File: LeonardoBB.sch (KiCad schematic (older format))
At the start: 39 parts, among them J1 USB_B_Micro, J2 Conn_01x17, J3 Conn_01x17, J4 I2C, Q1 Q_PMOS_GSD, Q2 Q_DUAL_PMOS_S1G1D2S2G2D1, SW1 SW_SPDT, U1 ATmega32U4-MU, U2 LMV358, U3 NCP1117-5.0_SOT223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

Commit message: Change footprints for USB and LMV358
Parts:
- J1: footprint Connector_USB:USB_Micro-B_Amphenol_10103594-0001LF_Horizontal -> Connector_USB:USB_Micro-B_Molex-105017-0001
- U2: footprint Package_SO:VSSOP-8_2.3x2mm_P0.5mm -> Package_SO:VSSOP-8_3.0x3.0mm_P0.65mm
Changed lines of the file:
@@
 EESchema Schematic File Version 4
+LIBS:LeonardoBB-cache
 EELAYER 26 0
 EELAYER END
@@
 F 0 "J1" H 2505 6767 50  0000 C CNN
 F 1 "USB_B_Micro" H 2505 6676 50  0000 C CNN
-F 2 "Connector_USB:USB_Micro-B_Amphenol_10103594-0001LF_Horizontal" H 2600 6250 50  0001 C CNN
+F 2 "Connector_USB:USB_Micro-B_Molex-105017-0001" H 2600 6250 50  0001 C CNN
 F 3 "~" H 2600 6250 50  0001 C CNN
 	1    2450 6300
@@
 F 0 "U2" H 6400 2817 50  0000 C CNN
 F 1 "LMV358" H 6400 2726 50  0000 C CNN
-F 2 "Package_SO:VSSOP-8_2.3x2mm_P0.5mm" H 6400 2450 50  0001 C CNN
+F 2 "Package_SO:VSSOP-8_3.0x3.0mm_P0.65mm" H 6400 2450 50  0001 C CNN
 F 3 "http://www.ti.com/lit/ds/symlink/lmv324.pdf" H 6400 2450 50  0001 C CNN
 	1    6400 2450
@@
 F 0 "U2" H 6250 4617 50  0000 C CNN
 F 1 "LMV358" H 6250 4526 50  0000 C CNN
-F 2 "Package_SO:VSSOP-8_2.3x2mm_P0.5mm" H 6250 4250 50  0001 C CNN
+F 2 "Package_SO:VSSOP-8_3.0x3.0mm_P0.65mm" H 6250 4250 50  0001 C CNN
 F 3 "http://www.ti.com/lit/ds/symlink/lmv324.pdf" H 6250 4250 50  0001 C CNN
 	2    6250 4250
@@
 F 0 "U2" H 5358 2896 50  0000 L CNN
 F 1 "LMV358" H 5358 2805 50  0000 L CNN
-F 2 "Package_SO:VSSOP-8_2.3x2mm_P0.5mm" H 5400 2850 50  0001 C CNN
+F 2 "Package_SO:VSSOP-8_3.0x3.0mm_P0.65mm" H 5400 2850 50  0001 C CNN
 F 3 "http://www.ti.com/lit/ds/symlink/lmv324.pdf" H 5400 2850 50  0001 C CNN
 	3    5400 2850

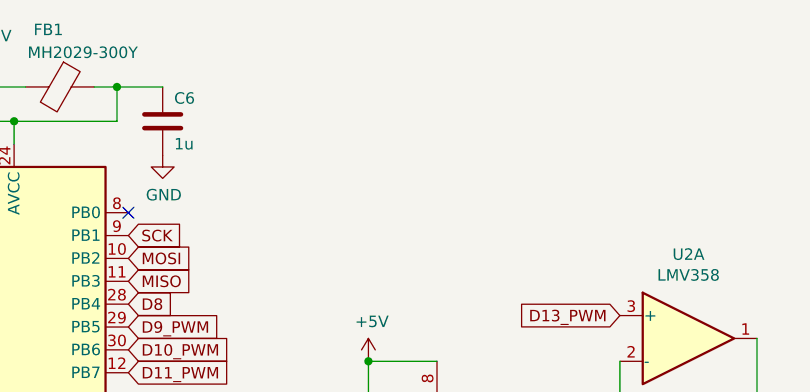
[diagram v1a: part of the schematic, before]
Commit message: Add reset switch
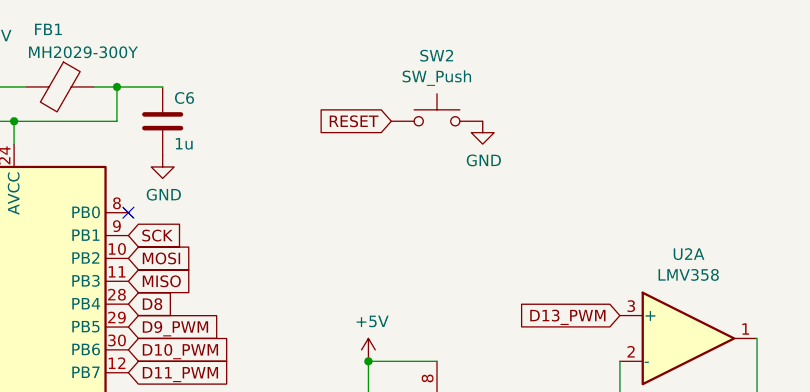
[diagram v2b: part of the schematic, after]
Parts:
- added SW2: SW_Push, Button_Switch_SMD:SW_SPST_PTS810, symbol Switch:SW_Push
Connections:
- net GND: now also SW2.2
- net RESET: now also SW2.1
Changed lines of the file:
@@
 Connection ~ 7650 6100
 Connection ~ 7650 5650
+$Comp
+L Switch:SW_Push SW2
+U 1 1 5C8FDE43
+P 5300 1500
+F 0 "SW2" H 5300 1785 50  0000 C CNN
+F 1 "SW_Push" H 5300 1694 50  0000 C CNN
+F 2 "Button_Switch_SMD:SW_SPST_PTS810" H 5300 1700 50  0001 C CNN
+F 3 "~" H 5300 1700 50  0001 C CNN
+	1    5300 1500
+	1    0    0    -1
+$EndComp
+Text GLabel 5100 1500 0    50   Input ~ 0
+RESET
+$Comp
+L power:GND #PWR0134
+U 1 1 5C8FDF29
+P 5500 1500
+F 0 "#PWR0134" H 5500 1250 50  0001 C CNN
+F 1 "GND" H 5505 1327 50  0000 C CNN
+F 2 "" H 5500 1500 50  0001 C CNN
+F 3 "" H 5500 1500 50  0001 C CNN
+	1    5500 1500
+	1    0    0    -1
+$EndComp
 $EndSCHEMATC
